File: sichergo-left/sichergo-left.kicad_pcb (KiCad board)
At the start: 2 copper layers, 118.1 x 98.8 mm, 92 parts, among them J1 Conn_01x04_Pin, Q1 2N7002, SW1 SW_Push, SW10 SW_Push, SW11 SW_Push, SW12 SW_Push, SW13 SW_Push, SW14 SW_Push, SW15 SW_Push, SW16 SW_Push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

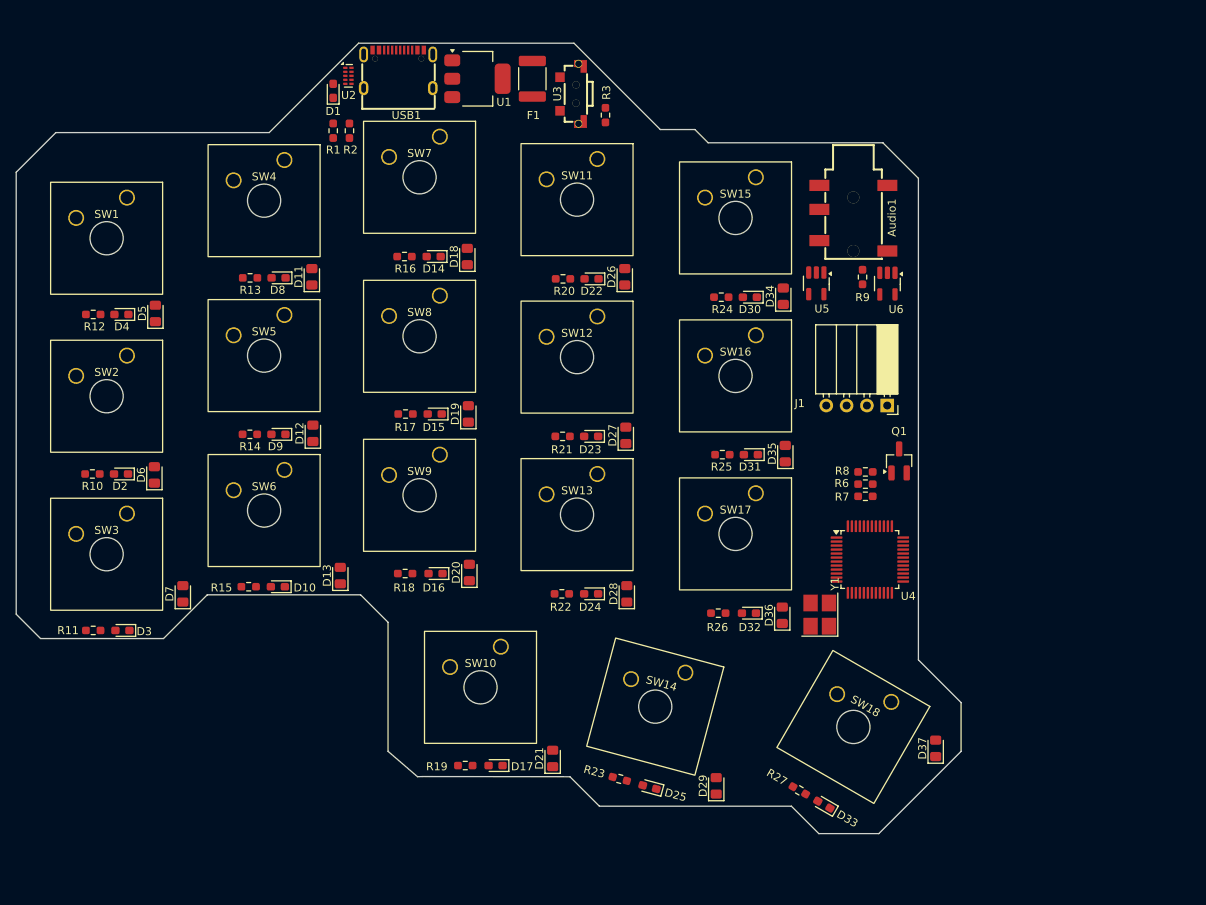
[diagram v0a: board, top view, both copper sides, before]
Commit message: Route left side
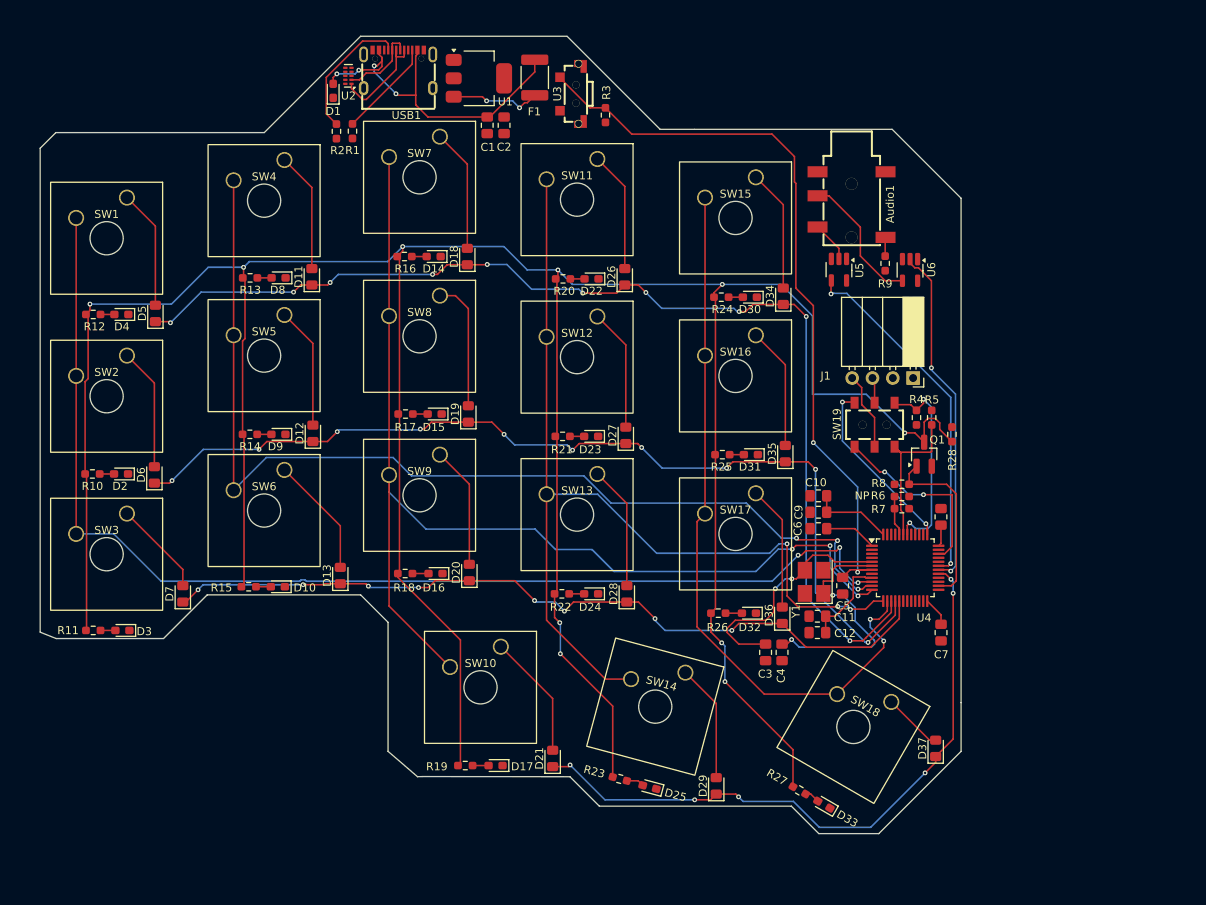
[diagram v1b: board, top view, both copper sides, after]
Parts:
- added C1: 10 µF, Capacitor_SMD:C_0805_2012Metric_Pad1.18x1.45mm_HandSolder, F.Cu at (145.9, 64.9)
- added C10: 10 µF, Capacitor_SMD:C_0805_2012Metric_Pad1.18x1.45mm_HandSolder, F.Cu at (187.3, 111.2)
- added C11: 0.1 µF, Capacitor_SMD:C_0805_2012Metric_Pad1.18x1.45mm_HandSolder, F.Cu at (187.1, 126.2)
- added C12: 1 µF, Capacitor_SMD:C_0805_2012Metric_Pad1.18x1.45mm_HandSolder, F.Cu at (187.1, 128.3)
- added C2: 22 µF, Capacitor_SMD:C_0805_2012Metric_Pad1.18x1.45mm_HandSolder, F.Cu at (148.0, 64.9)
- added C3: 10 pF, Capacitor_SMD:C_0805_2012Metric_Pad1.18x1.45mm_HandSolder, F.Cu at (180.7, 130.8)
- added C4: 10 pF, Capacitor_SMD:C_0805_2012Metric_Pad1.18x1.45mm_HandSolder, F.Cu at (182.7, 130.8)
- added C5: 0.1 µF, Capacitor_SMD:C_0805_2012Metric_Pad1.18x1.45mm_HandSolder, F.Cu at (190.3, 122.4)
- added C6: 0.1 µF, Capacitor_SMD:C_0805_2012Metric_Pad1.18x1.45mm_HandSolder, F.Cu at (187.3, 115.3)
- added C7: 0.1 µF, Capacitor_SMD:C_0805_2012Metric_Pad1.18x1.45mm_HandSolder, F.Cu at (202.6, 128.3)
- added C8: 0.1 µF, Capacitor_SMD:C_0805_2012Metric_Pad1.18x1.45mm_HandSolder, F.Cu at (202.6, 113.8)
- added C9: 0.1 µF, Capacitor_SMD:C_0805_2012Metric_Pad1.18x1.45mm_HandSolder, F.Cu at (187.3, 113.2)
- added R28: 4.7 kohm, Resistor_SMD:R_0603_1608Metric_Pad0.98x0.95mm_HandSolder, F.Cu at (204.0, 103.5)
- added R4: 4.7 kohm, Resistor_SMD:R_0603_1608Metric_Pad0.98x0.95mm_HandSolder, F.Cu at (199.5, 101.4)
- added R5: 4.7 kohm, Resistor_SMD:R_0603_1608Metric_Pad0.98x0.95mm_HandSolder, F.Cu at (201.4, 101.4)
- added SW19: MS-22C01-G010, easyeda2kicad:SW-SMD_6P-L7.2-W3.5-P2.50-LS6.0-TL, F.Cu at (194.3, 102.3)
- moved R6 4.81 mm to (197.7, 111.3)
- moved R8 4.81 mm to (197.7, 109.7)
- moved R7 4.81 mm to (197.7, 112.8)
- moved J1 4.72 mm to (199.1, 96.5)
- moved U4 4.55 mm to (198.1, 120.2)
- moved Y1 4.15 mm to (186.7, 121.9)
- moved U5 3.30 mm to (189.8, 82.9)
- moved R9 3.30 mm to (195.6, 82.1)
- moved U6 3.30 mm to (198.7, 83.0)
- moved Q1 3.25 mm to (200.5, 106.0)
- moved R1 2.41 mm to (129.0, 65.6)
- moved Audio1 1.72 mm to (191.4, 74.8)
- moved R2 1.63 mm to (127.0, 65.6)
- moved F1 0.34 mm to (151.8, 58.9)
- moved U1 0.18 mm to (144.8, 59.0)
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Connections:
- Q1 pad 3: +3V3 -> /MatrixL/LED_DRIVE
- R10 pad 1: +3V3 -> /MatrixL/LED_DRIVE
- R11 pad 1: +3V3 -> /MatrixL/LED_DRIVE
- R12 pad 1: +3V3 -> /MatrixL/LED_DRIVE
- R13 pad 1: +3V3 -> /MatrixL/LED_DRIVE
- R14 pad 1: +3V3 -> /MatrixL/LED_DRIVE
- R15 pad 1: +3V3 -> /MatrixL/LED_DRIVE
- R16 pad 1: +3V3 -> /MatrixL/LED_DRIVE
- R17 pad 1: +3V3 -> /MatrixL/LED_DRIVE
- R18 pad 1: +3V3 -> /MatrixL/LED_DRIVE
- R19 pad 1: +3V3 -> /MatrixL/LED_DRIVE
- R20 pad 1: +3V3 -> /MatrixL/LED_DRIVE
- R21 pad 1: +3V3 -> /MatrixL/LED_DRIVE
- R22 pad 1: +3V3 -> /MatrixL/LED_DRIVE
- R23 pad 1: +3V3 -> /MatrixL/LED_DRIVE
- R24 pad 1: +3V3 -> /MatrixL/LED_DRIVE
- R25 pad 1: +3V3 -> /MatrixL/LED_DRIVE
- R26 pad 1: +3V3 -> /MatrixL/LED_DRIVE
- R27 pad 1: +3V3 -> /MatrixL/LED_DRIVE
- U4 pad 32: unconnected-(U4-PA11-Pad32) -> /D-
- U4 pad 33: unconnected-(U4-PA12-Pad33) -> /D+
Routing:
- net /MatrixL/LED_DRIVE: track 0.00 -> 416.3 mm, vias 0 -> 10
- net /KB_COL_0: track 0.00 -> 146.7 mm, vias 0 -> 3
- net /KB_ROW_0: track 0.00 -> 140.1 mm, vias 0 -> 10
- net /KB_COL_2: track 0.00 -> 139.5 mm, vias 0 -> 3
- net /KB_COL_1: track 0.00 -> 129.7 mm, vias 0 -> 3
- net /KB_COL_3: track 0.00 -> 122.1 mm, vias 0 -> 3
- net /KB_ROW_1: track 0.00 -> 120.7 mm, vias 0 -> 10
- net /KB_ROW_2: track 0.00 -> 100.0 mm, vias 0 -> 8
- net Net-(U4-NRST): track 0.00 -> 94.7 mm, vias 0 -> 2
- net /KB_COL_4: track 0.00 -> 92.1 mm, vias 0 -> 2
- net /KB_ROW_3: track 0.00 -> 80.9 mm, vias 0 -> 6
- net /VBUS: track 0.00 -> 44.8 mm, vias 0 -> 4
- net /UART_RX: track 0.00 -> 44.5 mm, vias 0 -> 2
- net /UART_TX: track 0.00 -> 43.5 mm, vias 0 -> 2
- net +3V3: track 0.00 -> 34.6 mm
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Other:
- board size 118.1 x 98.8 mm -> 115.1 x 99.7 mm
- board text added: "NP"

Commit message: Reroute everything
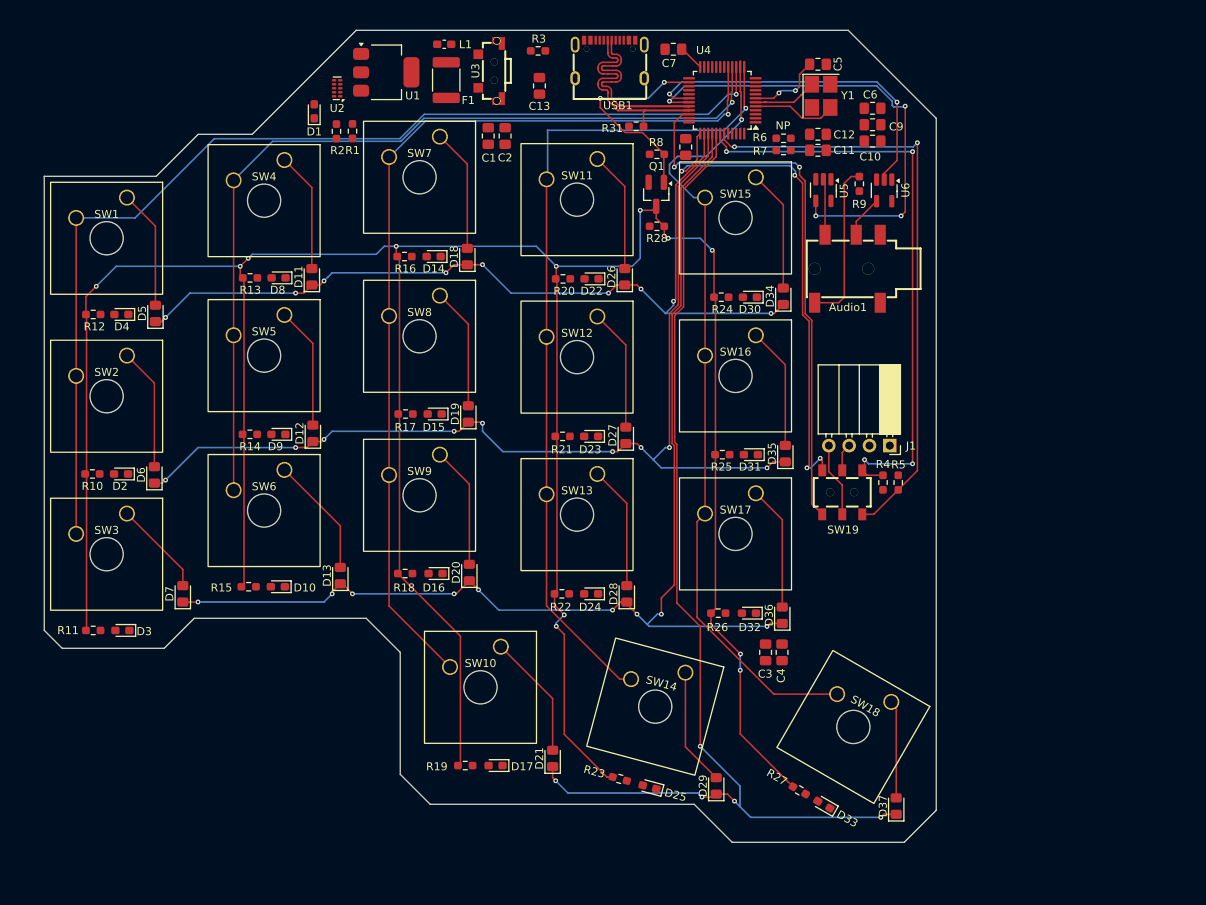
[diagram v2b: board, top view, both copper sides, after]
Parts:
- added C13: 10000 pF, Capacitor_SMD:C_0805_2012Metric_Pad1.18x1.45mm_HandSolder, F.Cu at (152.4, 59.9)
- added L1: 120 Ohm @ 100 MHz, Inductor_SMD:L_0603_1608Metric_Pad1.05x0.95mm_HandSolder, F.Cu at (140.5, 54.8)
- added R31: 1.5 kohm, Resistor_SMD:R_0603_1608Metric_Pad0.98x0.95mm_HandSolder, F.Cu at (164.5, 65.0)
- moved C7 80.2 mm to (169.1, 55.4), turned to 180 degrees
- moved C5 65.2 mm to (187.2, 57.2), turned to 0 degrees
- moved U4 62.8 mm to (175.2, 61.8), turned to 180 degrees
- moved C12 62.3 mm to (187.2, 66.0), turned to 0 degrees
- moved Y1 60.7 mm to (187.6, 61.2), turned to -90 degrees
- moved C11 58.2 mm to (187.2, 68.0), turned to 0 degrees
- moved C8 56.2 mm to (170.7, 67.6), turned to -90 degrees
- moved C6 53.0 mm to (194.0, 62.8), turned to 0 degrees
- moved R8 51.4 mm to (167.1, 68.5)
- moved C9 48.9 mm to (194.0, 64.8), turned to 0 degrees
- moved R6 47.2 mm to (182.9, 66.5)
- moved R7 47.2 mm to (182.9, 68.0)
- moved Q1 46.7 mm to (167.0, 73.5), turned to -90 degrees
- moved R28 45.1 mm to (167.1, 77.5), turned to 180 degrees
- moved C10 44.8 mm to (194.0, 66.9), turned to 0 degrees
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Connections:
- C1 pad 1: /VBUS -> Net-(C1-Pad1)
- F1 pad 1: /VBUS -> Net-(C1-Pad1)
- U4 pad 10: /KB_COL_0 -> unconnected-(U4-PA0-Pad10)
- U4 pad 11: /KB_COL_1 -> unconnected-(U4-PA1-Pad11)
- U4 pad 12: /KB_COL_2 -> unconnected-(U4-PA2-Pad12)
- U4 pad 15: /KB_ROW_0 -> /KB_COL_0
- U4 pad 16: /KB_ROW_1 -> /KB_COL_1
- U4 pad 17: /KB_ROW_2 -> /KB_COL_2
- U4 pad 29: /KB_ROW_3 -> unconnected-(U4-PA8-Pad29)
- U4 pad 38: unconnected-(U4-PA15-Pad38) -> /KB_ROW_0
- U4 pad 39: unconnected-(U4-PB3-Pad39) -> /KB_ROW_1
- U4 pad 40: unconnected-(U4-PB4-Pad40) -> /KB_ROW_2
- U4 pad 41: unconnected-(U4-PB5-Pad41) -> /KB_ROW_3
- USB1 pad 13: GND -> Net-(C13-Pad1)
- USB1 pad 14: GND -> Net-(C13-Pad1)
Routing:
- net Net-(U4-NRST): track 94.7 -> 9.42 mm
- net /KB_ROW_3: track 80.9 -> 136.5 mm, vias 6 -> 5
- net /OLED_SDA: track 20.7 -> 75.6 mm, vias 0 -> 2
- net /OLED_SCL: track 25.8 -> 75.4 mm, vias 2 -> 4
- net /KB_ROW_2: track 100.0 -> 146.0 mm, vias 8 -> 9
- net /SWDIO: track 23.3 -> 68.5 mm
- net /VBUS: track 44.8 -> 0.00 mm, vias 4 -> 0
- net /SWCLK: track 22.6 -> 62.5 mm, vias 2 -> 4
- net /MatrixL/LED_DRIVE: track 416.3 -> 383.8 mm, vias 10 -> 12
- net +3V3: track 34.6 -> 3.24 mm
- net /KB_ROW_0: track 140.1 -> 109.8 mm, vias 10 -> 9
- net Net-(U4-PD1): track 31.9 -> 8.25 mm, vias 2 -> 0
- net /KB_COL_2: track 139.5 -> 117.5 mm, vias 3 -> 1
- net /KB_COL_1: track 129.7 -> 109.6 mm, vias 3 -> 1
- net Net-(U4-PD0): track 30.4 -> 10.8 mm, vias 2 -> 0
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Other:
- board size 115.1 x 99.7 mm -> 111.5 x 101.5 mm

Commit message: FInish routing, missing 3V3 net
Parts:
- moved C4 74.8 mm to (186.4, 56.0), turned to 90 degrees
- moved C3 69.9 mm to (191.0, 61.6), turned to 90 degrees
- moved U2 27.9 mm to (154.6, 55.1)
- moved R1 26.5 mm to (155.0, 60.5)
- moved R2 26.3 mm to (152.8, 60.5)
- moved C2 18.6 mm to (132.6, 56.0), turned to 180 degrees
- moved D1 14.7 mm to (137.0, 55.8)
- moved C5 5.23 mm to (182.0, 56.8), turned to 90 degrees
- moved U1 4.11 mm to (130.2, 61.0)
- moved C13 1.99 mm to (150.6, 60.8)
- moved R3 0.54 mm to (151.7, 55.6)
- moved F1 0.18 mm to (140.8, 59.4)
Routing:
- net Net-(U4-NRST): track 9.42 -> 50.4 mm, vias 2 -> 4
- net /VBUS: track 0.00 -> 31.0 mm, vias 0 -> 3
- net Net-(C13-Pad1): track 0.00 -> 24.6 mm, vias 0 -> 1
- net Net-(U1-VI): track 0.00 -> 16.4 mm, vias 0 -> 2
- net Net-(C1-Pad1): track 0.00 -> 14.4 mm
- net Net-(USB1-CC2): track 0.00 -> 13.1 mm, vias 0 -> 2
- net /D-: track 25.4 -> 36.1 mm, vias 0 -> 3
- net Net-(USB1-CC1): track 0.00 -> 10.5 mm, vias 0 -> 2
- net /D+: track 28.3 -> 37.7 mm, vias 0 -> 2
- net Net-(U4-BOOT0): track 0.00 -> 9.04 mm, vias 0 -> 2
- net +3V3: track 3.24 -> 8.36 mm
- net Net-(U4-PD1): track 8.25 -> 11.0 mm
- net /OLED_SDA: track 75.6 -> 78.1 mm
- net Net-(U4-PD0): track 10.8 -> 13.1 mm
- net Net-(D25-A): track 0.00 -> 2.23 mm
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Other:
- board size 111.5 x 101.5 mm -> 111.5 x 102.7 mm

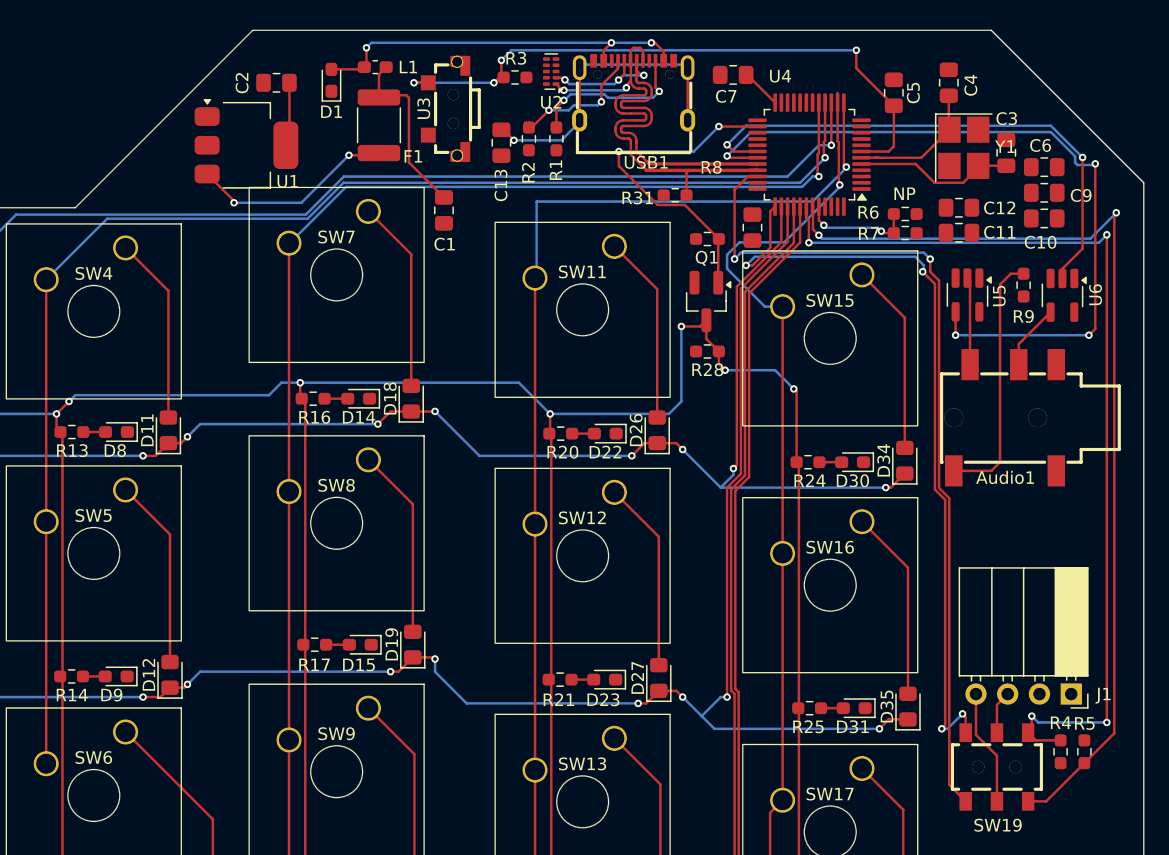
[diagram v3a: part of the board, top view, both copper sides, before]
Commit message: Finish 3V3
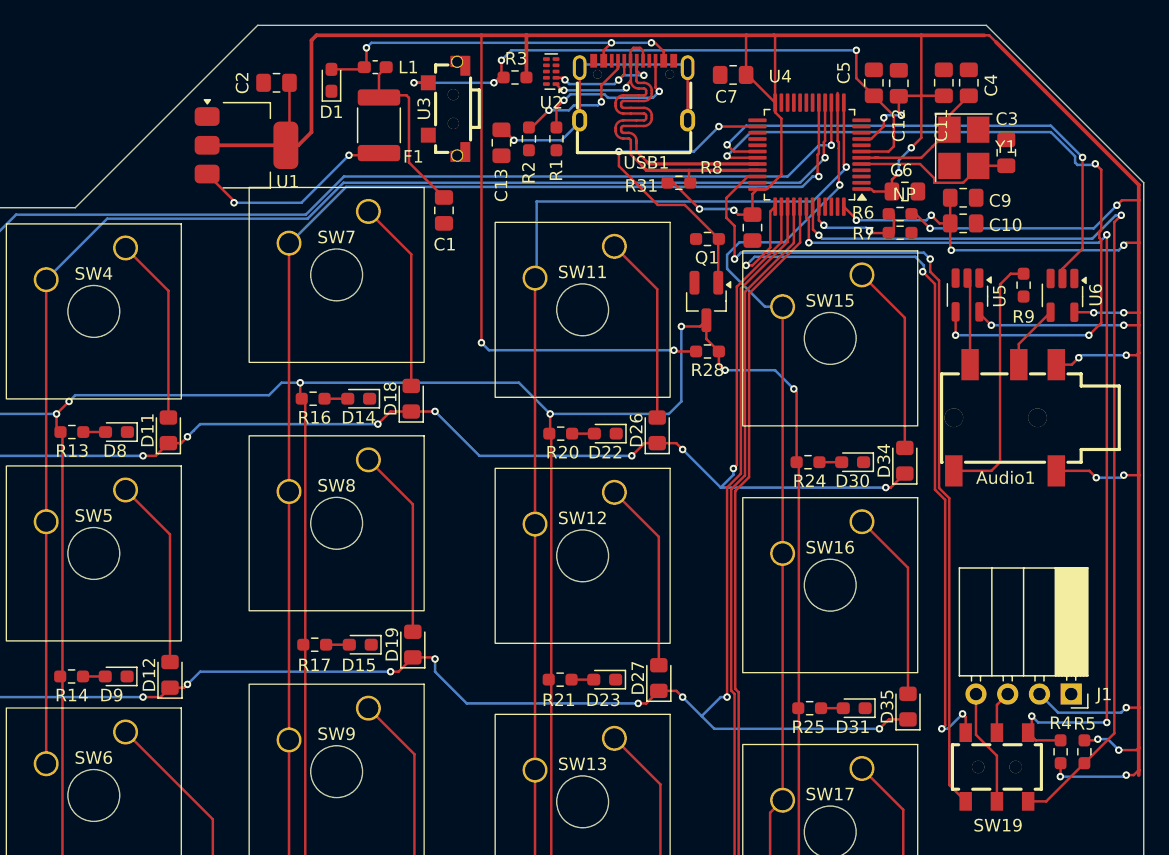
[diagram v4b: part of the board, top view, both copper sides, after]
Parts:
- moved C11 12.1 mm to (186.0, 56.0), turned to 90 degrees
- moved C6 11.3 mm to (182.9, 64.7)
- moved C12 11.1 mm to (182.4, 56.0), turned to 90 degrees
- moved C9 6.50 mm to (187.6, 65.2)
- moved C10 6.50 mm to (187.6, 67.2)
- moved C5 1.79 mm to (180.4, 56.0)
- moved C4 1.60 mm to (188.0, 56.0)
- moved R31 1.04 mm to (164.8, 64.0)
- moved R7 0.41 mm to (182.5, 68.0)
- moved R6 0.41 mm to (182.5, 66.5)
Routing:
- net +3V3: track 8.36 -> 342.9 mm, vias 0 -> 27
- net /D+: track 37.7 -> 36.6 mm
- net Net-(U4-PD1): track 11.0 -> 11.6 mm
- net /SWDIO: track 68.5 -> 69.0 mm
- net /UART_RX: track 60.6 -> 61.2 mm
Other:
- board size 111.5 x 102.7 mm -> 111.5 x 103.1 mm
